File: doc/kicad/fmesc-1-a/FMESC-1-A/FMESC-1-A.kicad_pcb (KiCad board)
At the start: 2 copper layers, 48 x 48 mm, 106 parts, among them Q1 AON6504, Q10 AON6504, Q11 AON6504, Q12 AON6504, Q13 AON6504, Q14 AON6504, Q15 AON6504, Q16 AON6504, Q17 AON6504, Q18 AON6504, Q19 AON6504, Q2 AON6504, Q20 AON6504, Q21 AON6504, Q22 AON6504, Q23 AON6504, Q24 AON6504, Q3 AON6504, Q4 AON6504, Q5 AON6504, Q6 AON6504, Q7 AON6504, Q8 AON6504, Q9 AON6504, U1 FD6288Q, U2 FD6288Q, U3 FD6288Q, U4 FD6288Q

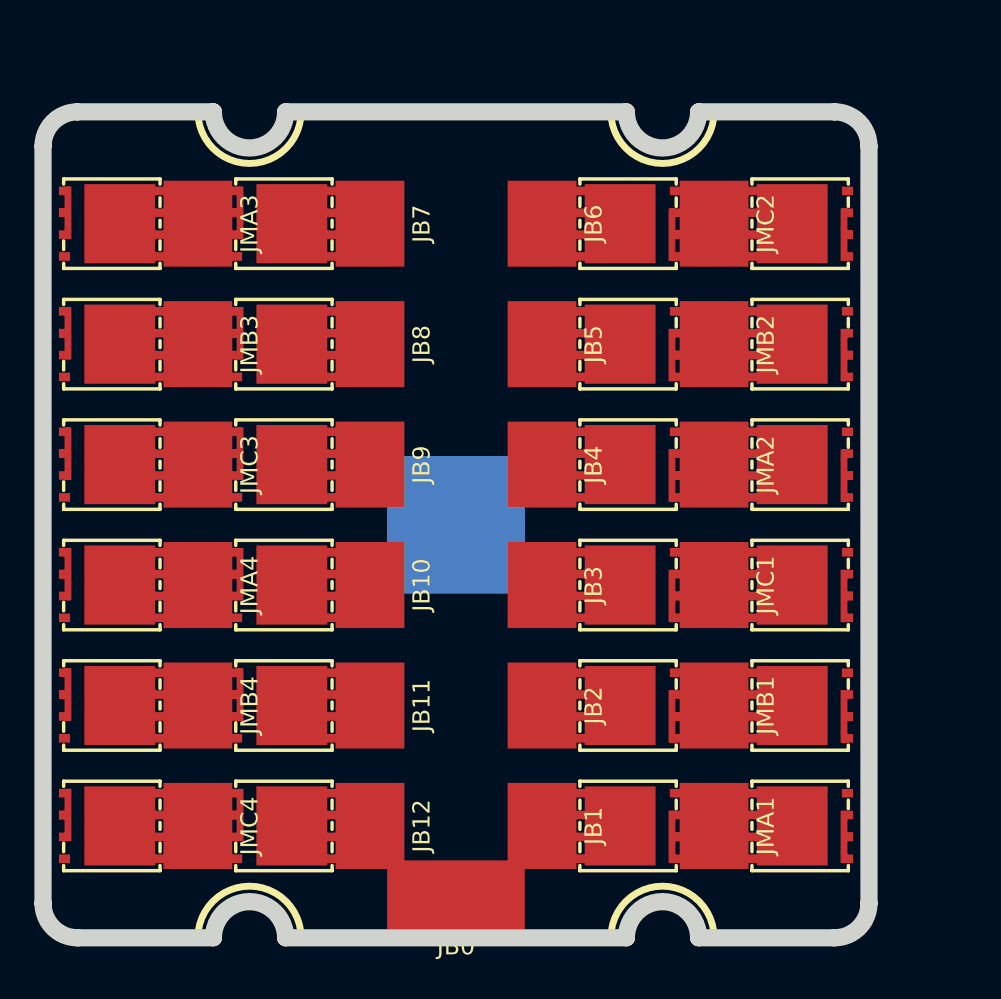
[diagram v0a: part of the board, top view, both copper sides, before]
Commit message: doc/kicad: FMESC-1-A  update PCB
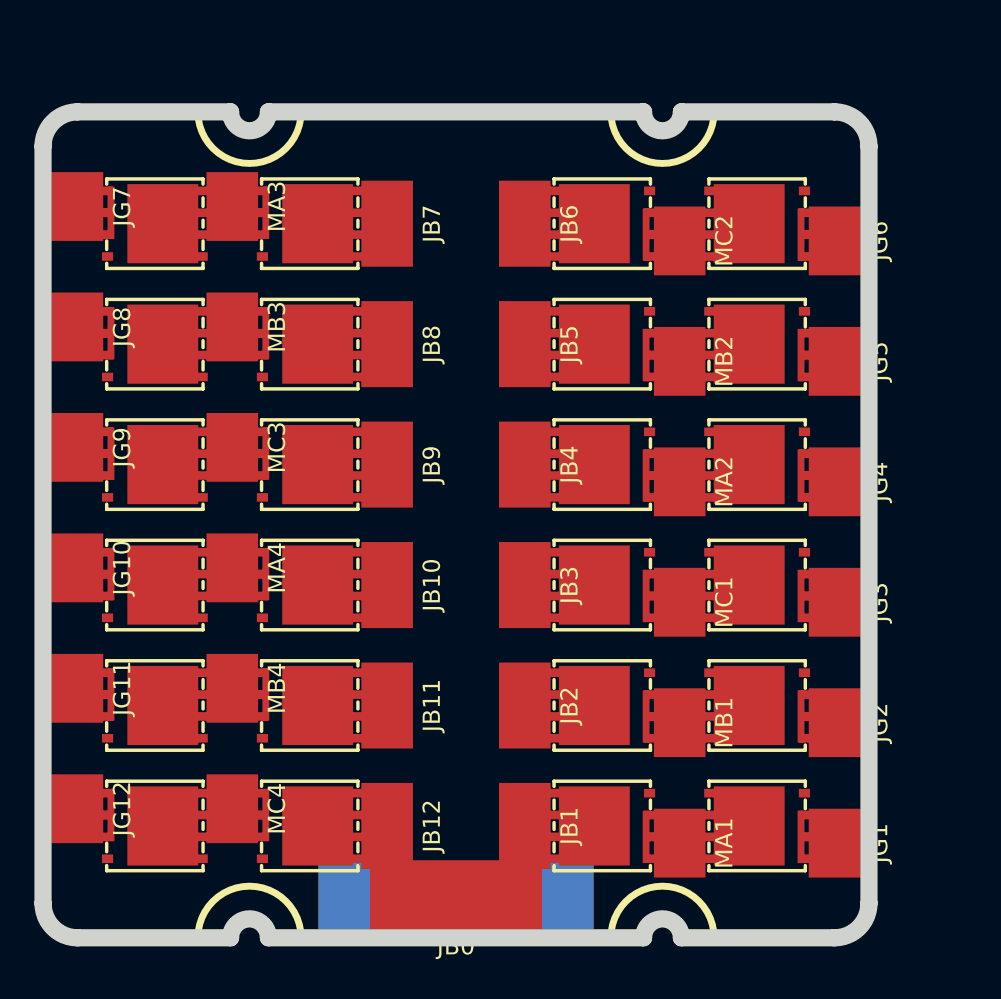
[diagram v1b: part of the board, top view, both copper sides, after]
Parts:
- added JG1: Conn_01x01, fmlibf:JS3x4mm, F.Cu at (96.0, 92.5)
- added JG10: Conn_01x01, fmlibf:JS3x4mm, F.Cu at (52.0, 76.5)
- added JG11: Conn_01x01, fmlibf:JS3x4mm, F.Cu at (52.0, 83.5)
- added JG12: Conn_01x01, fmlibf:JS3x4mm, F.Cu at (52.0, 90.5)
- added JG2: Conn_01x01, fmlibf:JS3x4mm, F.Cu at (96.0, 85.5)
- added JG3: Conn_01x01, fmlibf:JS3x4mm, F.Cu at (96.0, 78.5)
- added JG4: Conn_01x01, fmlibf:JS3x4mm, F.Cu at (96.0, 71.5)
- added JG5: Conn_01x01, fmlibf:JS3x4mm, F.Cu at (96.0, 64.5)
- added JG6: Conn_01x01, fmlibf:JS3x4mm, F.Cu at (96.0, 57.5)
- added JG7: Conn_01x01, fmlibf:JS3x4mm, F.Cu at (52.0, 55.5)
- added JG8: Conn_01x01, fmlibf:JS3x4mm, F.Cu at (52.0, 62.5)
- added JG9: Conn_01x01, fmlibf:JS3x4mm, F.Cu at (52.0, 69.5)
- JB0: footprint fmlibf:JS4x8mm -> fmlibf:JS4x10mm
- JB1, JB10, JB11, JB12, JB2, JB3, JB4, JB5, JB6, JB7, JB8, JB9: footprint fmlibf:JS4x5mm -> fmlibf:JS3x5mm
- JG0: footprint fmlibf:JS8x8mm -> fmlibf:JS4x16mm
- MA1: renamed from JMA1; footprint fmlibf:JS4x5mm -> fmlibf:JS3x4mm
- MA2: renamed from JMA2; footprint fmlibf:JS4x5mm -> fmlibf:JS3x4mm
- MA3: renamed from JMA3; footprint fmlibf:JS4x5mm -> fmlibf:JS3x4mm
- MA4: renamed from JMA4; footprint fmlibf:JS4x5mm -> fmlibf:JS3x4mm
- MB1: renamed from JMB1; footprint fmlibf:JS4x5mm -> fmlibf:JS3x4mm
- MB2: renamed from JMB2; footprint fmlibf:JS4x5mm -> fmlibf:JS3x4mm
- MB3: renamed from JMB3; footprint fmlibf:JS4x5mm -> fmlibf:JS3x4mm
- MB4: renamed from JMB4; footprint fmlibf:JS4x5mm -> fmlibf:JS3x4mm
- MC1: renamed from JMC1; footprint fmlibf:JS4x5mm -> fmlibf:JS3x4mm
- MC2: renamed from JMC2; footprint fmlibf:JS4x5mm -> fmlibf:JS3x4mm
- MC3: renamed from JMC3; footprint fmlibf:JS4x5mm -> fmlibf:JS3x4mm
- MC4: renamed from JMC4; footprint fmlibf:JS4x5mm -> fmlibf:JS3x4mm
- moved JG0 21.5 mm to (74.0, 95.5)
- moved Q1 2.50 mm to (91.5, 91.5)
- moved Q11 2.50 mm to (91.5, 56.5)
- moved Q13 2.50 mm to (56.5, 56.5)
- moved Q15 2.50 mm to (56.5, 63.5)
- moved Q17 2.50 mm to (56.5, 70.5)
- moved Q19 2.50 mm to (56.5, 77.5)
- moved Q21 2.50 mm to (56.5, 84.5)
- moved Q23 2.50 mm to (56.5, 91.5)
- moved Q3 2.50 mm to (91.5, 84.5)
- moved Q5 2.50 mm to (91.5, 77.5)
- moved Q7 2.50 mm to (91.5, 70.5)
- moved Q9 2.50 mm to (91.5, 63.5)
- moved MA1 2.24 mm to (87.0, 92.5)
- moved MA2 2.24 mm to (87.0, 71.5)
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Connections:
- JB1 pad 1: /M1/VB -> +BATT
- JB10 pad 1: /M4/VB -> +BATT
- JB11 pad 1: /M4/VB -> +BATT
- JB12 pad 1: /M4/VB -> +BATT
- JB2 pad 1: /M1/VB -> +BATT
- JB3 pad 1: /M1/VB -> +BATT
- JB4 pad 1: /M2/VB -> +BATT
- JB5 pad 1: /M2/VB -> +BATT
- JB6 pad 1: /M2/VB -> +BATT
- JB7 pad 1: /M3/VB -> +BATT
- JB8 pad 1: /M3/VB -> +BATT
- JB9 pad 1: /M3/VB -> +BATT
- Q10 pad 1: /M2/VB -> +BATT
- Q12 pad 1: /M2/VB -> +BATT
- Q14 pad 1: /M3/VB -> +BATT
- Q16 pad 1: /M3/VB -> +BATT
- Q18 pad 1: /M3/VB -> +BATT
- Q2 pad 1: /M1/VB -> +BATT
- Q20 pad 1: /M4/VB -> +BATT
- Q22 pad 1: /M4/VB -> +BATT
- Q24 pad 1: /M4/VB -> +BATT
- Q4 pad 1: /M1/VB -> +BATT
- Q6 pad 1: /M1/VB -> +BATT
- Q8 pad 1: /M2/VB -> +BATT
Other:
- outline, holes or cut-outs redrawn

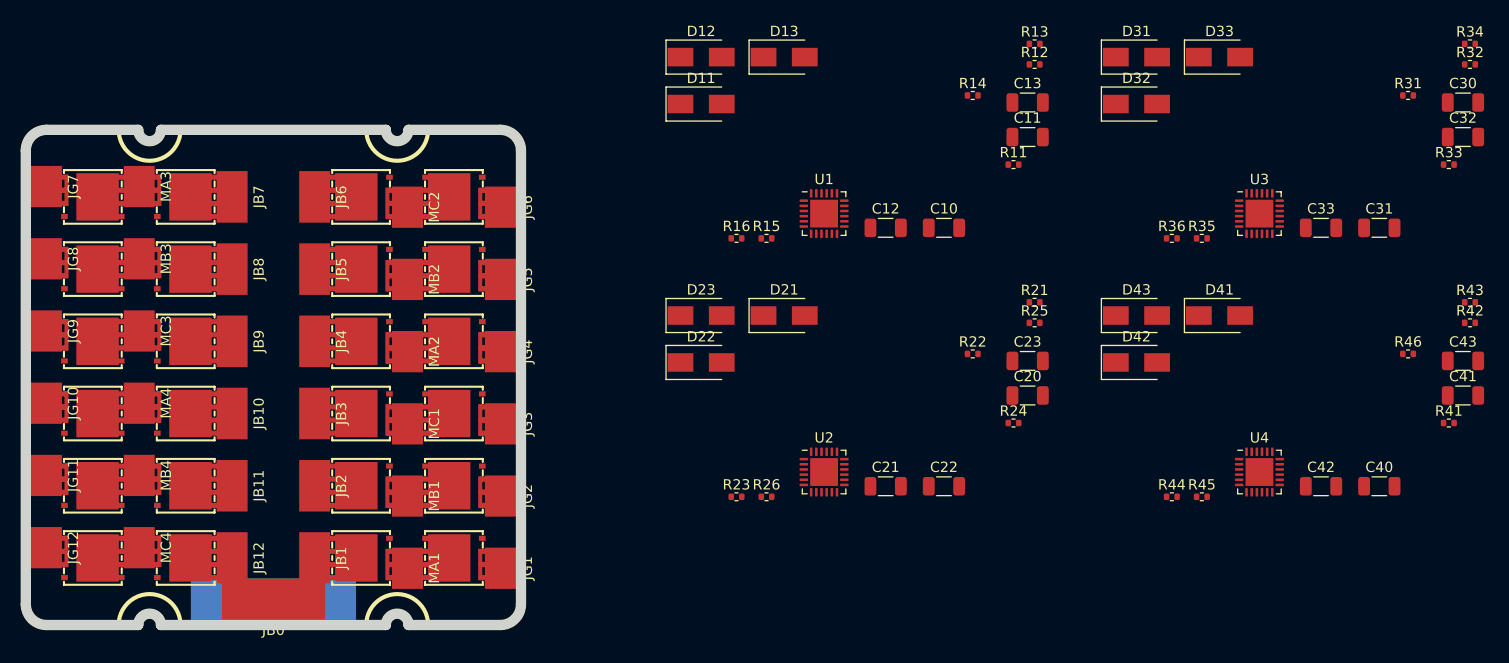
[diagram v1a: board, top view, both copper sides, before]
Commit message: doc/kicad: FMESC-1-A  first PCB layout
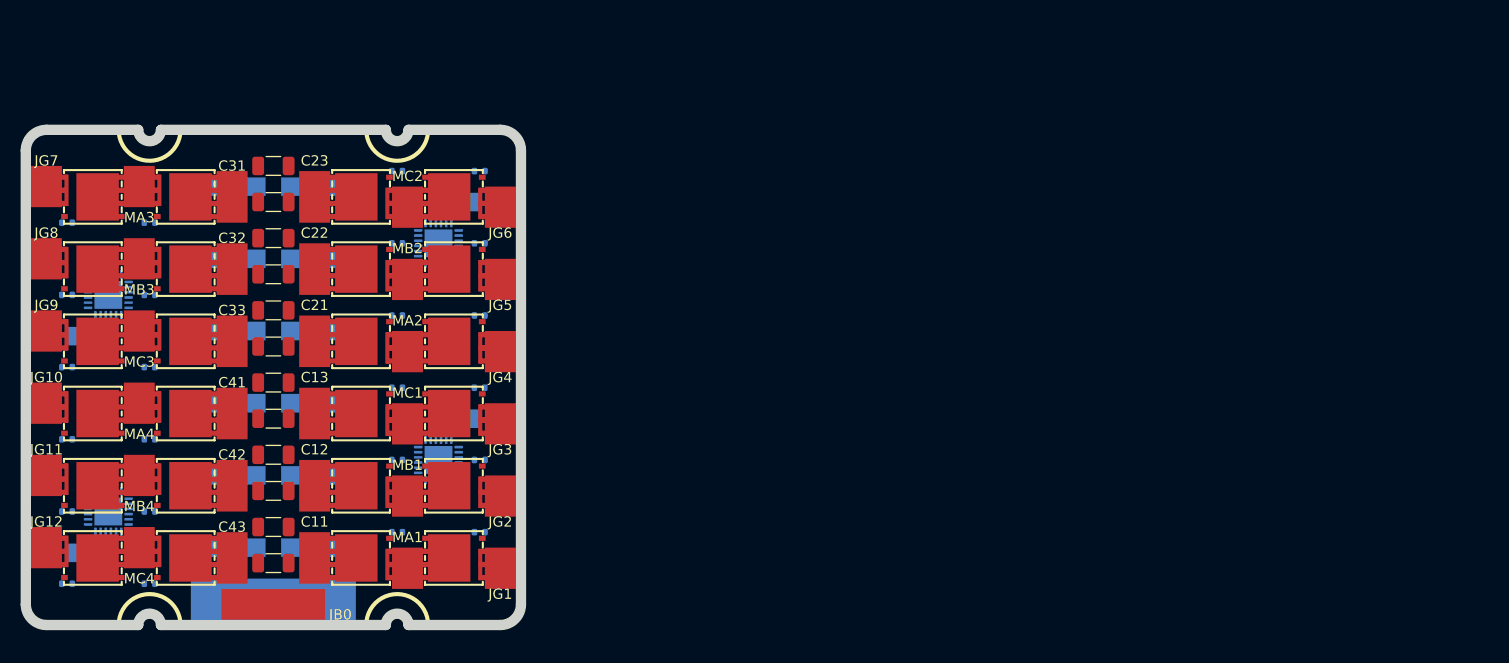
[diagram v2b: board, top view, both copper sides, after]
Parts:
- C10, C20, C30, C40, D11, D12, D13, D21, D22, D23, D31, D32, D33, D41, D42, D43, R11, R12, R13, R14, R15, R16, R21, R22, R23, R24, R25, R26, R31, R32, R33, R34, R35, R36, R41, R42, R43, R44, R45, R46, U1, U2, U3, U4: moved to B.Cu
- JB0: footprint fmlibf:JS4x10mm -> fmlibf:JS3x10mm
- moved R43 137.5 mm to (54.0, 87.0)
- moved C30 135.2 mm to (56.0, 70.0)
- moved R33 134.5 mm to (54.0, 66.0)
- moved R41 133.9 mm to (54.0, 80.0)
- moved R31 130.6 mm to (54.0, 59.0)
- moved R34 130.3 mm to (62.0, 66.0), turned to 180 degrees
- moved R32 128.9 mm to (62.0, 59.0), turned to 180 degrees
- moved R42 128.5 mm to (62.0, 80.0), turned to 180 degrees
- moved C40 125.4 mm to (56.0, 91.0)
- moved R46 124.0 mm to (62.0, 94.0), turned to 180 degrees
- moved C43 117.0 mm to (74.0, 92.0)
- moved C32 116.1 mm to (74.0, 64.0)
- moved C41 115.3 mm to (74.0, 78.0)
- moved U3 111.9 mm to (58.0, 66.0), turned to 90 degrees
- moved U4 111.6 mm to (58.0, 87.0), turned to 90 degrees
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
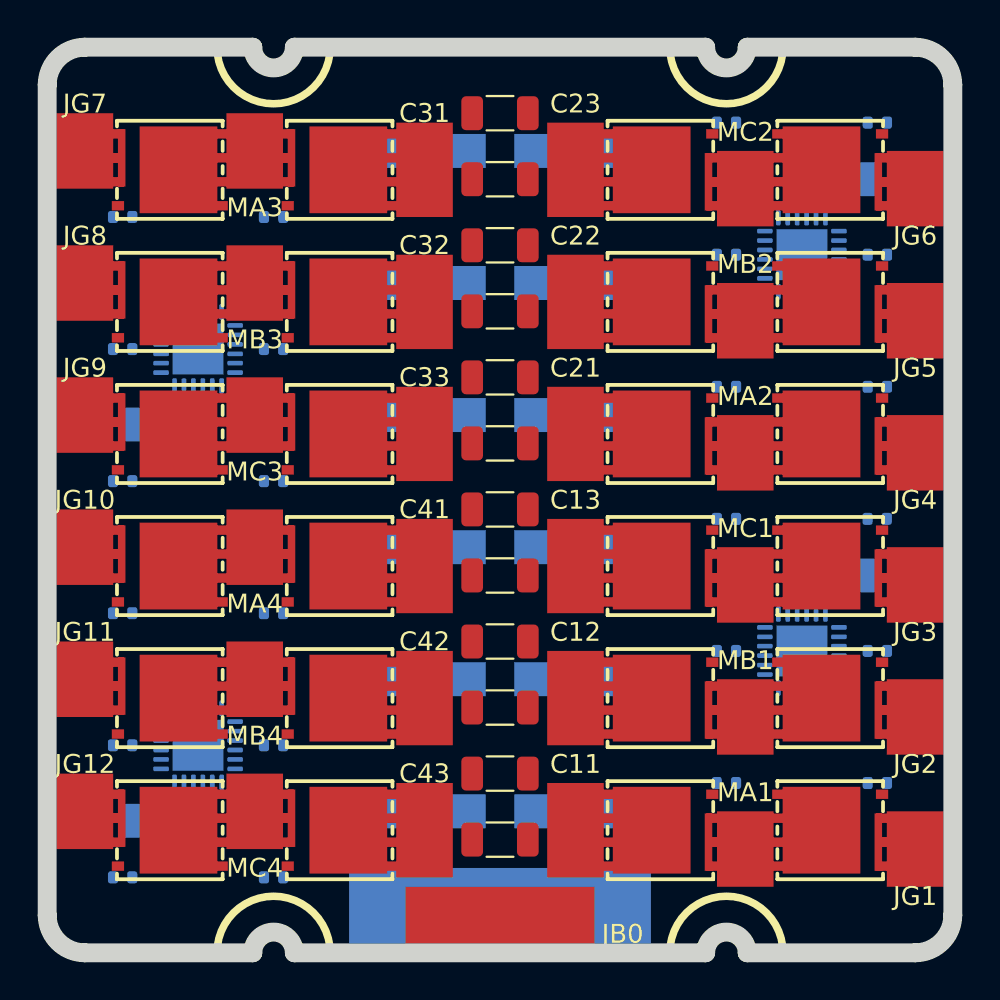
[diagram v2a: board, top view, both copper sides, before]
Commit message: doc/kicad: FMESC-1-A  PCB add wire (some)
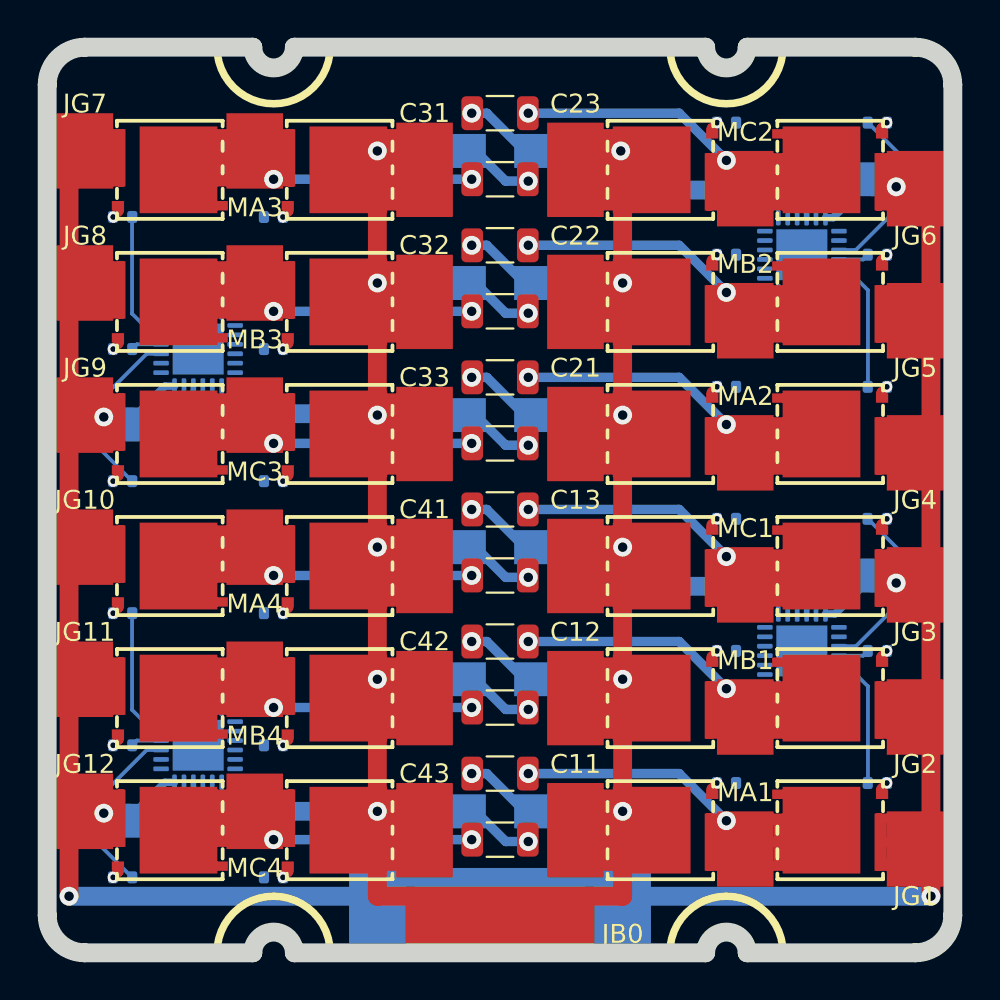
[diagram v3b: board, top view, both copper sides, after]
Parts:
- turned C31 to 180 degrees
- turned C32 to 180 degrees
- turned C33 to 180 degrees
- turned C41 to 180 degrees
- turned C42 to 180 degrees
- turned C43 to 180 degrees
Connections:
- C10 pad 2: /M1/VC -> +BATT
- C20 pad 2: /M2/VC -> +BATT
- C30 pad 2: /M3/VC -> +BATT
- C40 pad 2: /M4/VC -> +BATT
- D11 pad 2: /M1/VC -> +BATT
- D12 pad 2: /M1/VC -> +BATT
- D13 pad 2: /M1/VC -> +BATT
- D21 pad 2: /M2/VC -> +BATT
- D22 pad 2: /M2/VC -> +BATT
- D23 pad 2: /M2/VC -> +BATT
- D31 pad 2: /M3/VC -> +BATT
- D32 pad 2: /M3/VC -> +BATT
- D33 pad 2: /M3/VC -> +BATT
- D41 pad 2: /M4/VC -> +BATT
- D42 pad 2: /M4/VC -> +BATT
- D43 pad 2: /M4/VC -> +BATT
- U1 pad 4: /M1/VC -> +BATT
- U2 pad 4: /M2/VC -> +BATT
- U3 pad 4: /M3/VC -> +BATT
- U4 pad 4: /M4/VC -> +BATT
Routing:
- net +BATT: track 0.00 -> 269.2 mm, vias 0 -> 12
- net GND: track 0.00 -> 175.3 mm, vias 0 -> 6
- net /M1/A1: track 0.00 -> 24.6 mm, vias 0 -> 2
- net /M1/B1: track 0.00 -> 24.5 mm, vias 0 -> 2
- net /M2/C1: track 0.00 -> 23.8 mm, vias 0 -> 2
- net /M1/C1: track 0.00 -> 23.8 mm, vias 0 -> 2
- net /M2/A1: track 0.00 -> 23.8 mm, vias 0 -> 2
- net /M2/B1: track 0.00 -> 23.5 mm, vias 0 -> 2
- net /M4/B1: track 0.00 -> 23.3 mm, vias 0 -> 2
- net /M3/C1: track 0.00 -> 23.2 mm, vias 0 -> 2
- net /M4/C1: track 0.00 -> 23.1 mm, vias 0 -> 2
- net /M4/A1: track 0.00 -> 23.0 mm, vias 0 -> 2
- net /M3/B1: track 0.00 -> 23.0 mm, vias 0 -> 2
- net /M3/A1: track 0.00 -> 23.0 mm, vias 0 -> 2
- net /M2/CLG: track 0.00 -> 9.79 mm
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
